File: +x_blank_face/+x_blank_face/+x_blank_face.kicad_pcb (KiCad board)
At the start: 2 copper layers, 87 x 326.5 mm, 14 parts

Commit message: added schematic to +x and routed ish the schematic
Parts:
- added J1: Conn_01x08_Pin, CNN_GNSS_Footprint:DF13-8P, F.Cu at (194.3, 5.54)
- added J2: Conn_01x02_Pin, CNN_GNSS_Footprint:TE_440055-2, F.Cu at (195.2, 160.1)
- added J3: Conn_01x02_Pin, CNN_GNSS_Footprint:TE_440055-2, F.Cu at (194.0, 57.5)
- added R1: 75, CNN_GNSS_Footprint:UB3C-75RF1, F.Cu at (201.5, 36.8)
- added R2: 75, CNN_GNSS_Footprint:UB3C-75RF1, F.Cu at (188.7, 37.2)
- added R3: 75, CNN_GNSS_Footprint:UB3C-75RF1, F.Cu at (186.1, 133.0)
- added R4: 75, CNN_GNSS_Footprint:UB3C-75RF1, F.Cu at (204.0, 132.7)
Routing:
- added copper zone on F.Cu, net /+X Drain
- added copper zone on B.Cu, net /12VPDM

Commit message: Updated panels based on dxf drawings from mech, need to move all holes up 5mm
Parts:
- J1: moved to B.Cu
- moved R4 70.0 mm to (177.3, 197.4)
- moved R3 65.7 mm to (173.2, 197.4)
- moved J3 55.2 mm to (173.5, 6.32)
- moved R1 27.3 mm to (177.3, 49.4)
- moved J2 22.7 mm to (173.6, 153.0), turned to 0 degrees
- moved R2 19.7 mm to (173.2, 49.4)
- moved J1 15.3 mm to (196.5, 20.7), turned to 180 degrees
- moved H14 6.56 mm to (234.1, 94.1)
- moved H10 6.54 mm to (157.9, 94.1)
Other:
- outline, holes or cut-outs redrawn
- board text added: "${REFERENCE}"

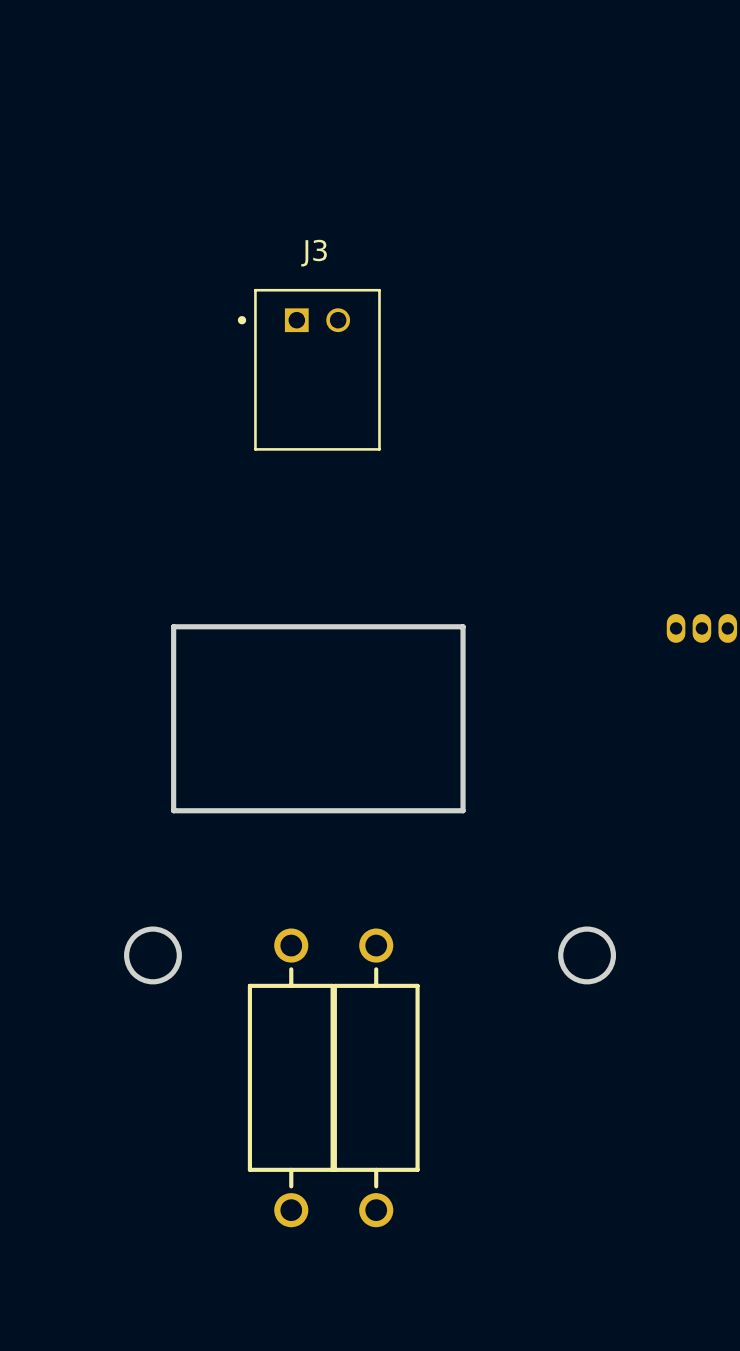
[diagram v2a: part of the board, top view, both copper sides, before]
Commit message: moved holes up 5mm, did what Jack said to do
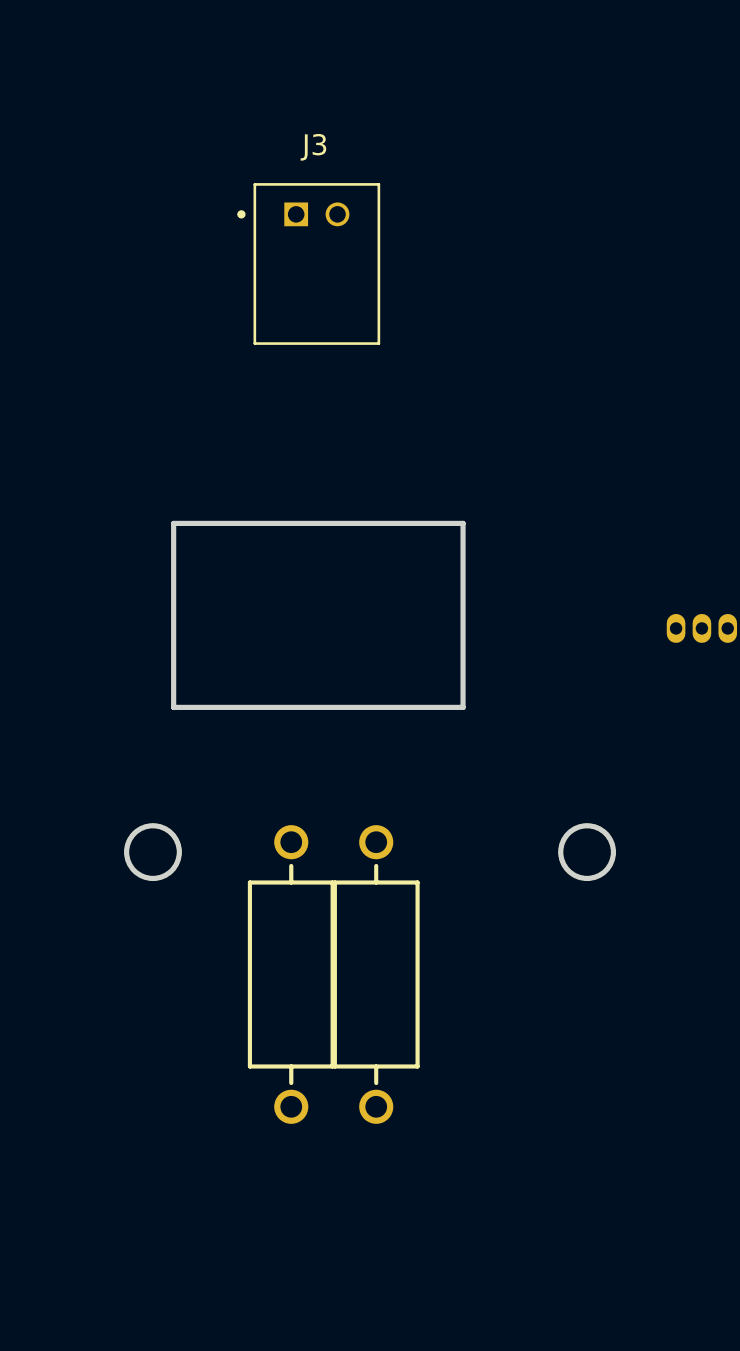
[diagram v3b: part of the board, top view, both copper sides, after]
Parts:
- moved J3 5.12 mm to (173.4, 1.20)
- moved R1 5.00 mm to (177.3, 44.4)
- moved R2 5.00 mm to (173.2, 44.4)
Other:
- outline, holes or cut-outs redrawn
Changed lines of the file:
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@@
 	(footprint "CNN_GNSS_Footprint:UB3C-75RF1"
 		(layer "F.Cu")
-		(at 177.31 49.371 90)
+		(at 177.31 44.371 90)
 		(descr "RES 50 OHM 1% 3W AXIAL")
 		(tags "Resistor")
@@
 	(footprint "CNN_GNSS_Footprint:UB3C-75RF1"
 		(layer "F.Cu")
-		(at 173.2 49.371 90)
+		(at 173.2 44.371 90)
 		(descr "RES 50 OHM 1% 3W AXIAL")
 		(tags "Resistor")
@@
 	(footprint "CNN_GNSS_Footprint:TE_440055-2"
 		(layer "F.Cu")
-		(at 173.4675 6.32)
+		(at 173.4375 1.2)
 		(property "Reference" "J3"
 			(at 0.925 -3.335 0)
@@
 	)
 	(gr_line
-		(start 167.51 21.15)
-		(end 181.51 21.15)
+		(start 167.51 16.15)
+		(end 181.51 16.15)
 		(stroke
 			(width 0.25)
@@
 	)
 	(gr_line
-		(start 181.51 30.05)
-		(end 181.51 21.15)
+		(start 181.51 25.05)
+		(end 181.51 16.15)
 		(stroke
 			(width 0.25)
@@
 	)
 	(gr_circle
-		(center 166.51 37.05)
-		(end 166.51 35.775)
+		(center 166.51 32.05)
+		(end 166.51 30.775)
 		(stroke
 			(width 0.25)
@@
 	)
 	(gr_circle
-		(center 187.51 37.05)
-		(end 187.51 35.775)
+		(center 187.51 32.05)
+		(end 187.51 30.775)
 		(stroke
 			(width 0.25)
@@
 	)
 	(gr_line
-		(start 167.51 30.05)
-		(end 181.51 30.05)
+		(start 167.51 25.05)
+		(end 181.51 25.05)
 		(stroke
 			(width 0.25)
@@
 	)
 	(gr_line
-		(start 167.51 30.05)
-		(end 167.51 21.15)
+		(start 167.51 25.05)
+		(end 167.51 16.15)
 		(stroke
 			(width 0.25)

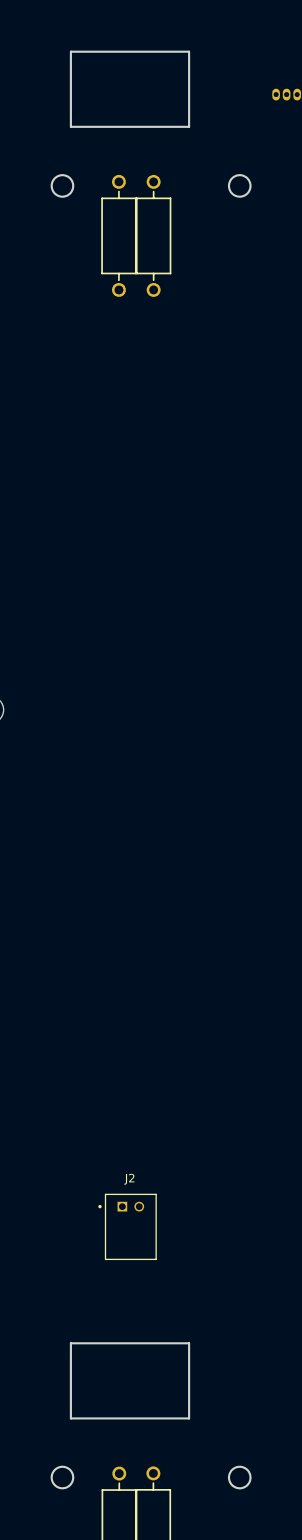
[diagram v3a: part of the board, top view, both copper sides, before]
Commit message: Moved some things around, locked some components
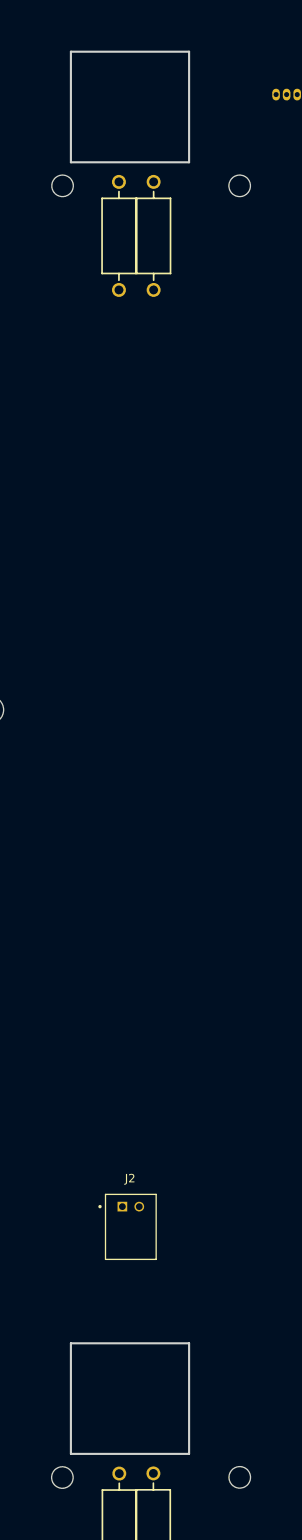
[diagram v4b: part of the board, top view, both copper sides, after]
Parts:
- added H1: MountingHole, CNN_GNSS_Footprint:2.55mm_Mounting_Hole, F.Cu at (187.5, 32.1)
- added H2: MountingHole, CNN_GNSS_Footprint:2.55mm_Mounting_Hole, F.Cu at (166.5, 32.1)
- added H3: MountingHole, CNN_GNSS_Footprint:2.55mm_Mounting_Hole, F.Cu at (166.5, 185.1)
- added H4: MountingHole, CNN_GNSS_Footprint:2.55mm_Mounting_Hole, F.Cu at (187.5, 185.1)
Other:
- outline, holes or cut-outs redrawn

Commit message: changed ALOT of things, got it to a point to send mech models,solar panel harness on BS need changed
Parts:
- J2, J3: moved to B.Cu
- moved J1 5.64 mm to (191.0, 21.7), turned to 0 degrees
- moved J3 5.30 mm to (175.8, -3.57), turned to 180 degrees
- moved J2 3.60 mm to (175.0, 149.7), turned to 180 degrees
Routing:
- net GND: track 0.00 -> 171.1 mm
- net /-X Serial Out: track 0.00 -> 169.8 mm

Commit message: I forgot what I changed
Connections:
- J1 pad 1: /12VPDM -> GND
- J1 pad 2: /12VPDM -> GND
- J1 pad 3: /+X Drain -> /-X Serial Out
- J1 pad 4: /+X Drain -> /-X Serial Out
- J1 pad 5: /-X Serial Out -> /+X Drain
- J1 pad 6: /-X Serial Out -> /+X Drain
- J1 pad 7: GND -> /12VPDM
- J1 pad 8: GND -> /12VPDM
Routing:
- net GND: track 171.1 -> 167.3 mm
- net /-X Serial Out: track 169.8 -> 168.3 mm
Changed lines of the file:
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@@
 			(remove_unused_layers no)
 			(roundrect_rratio 0.25)
-			(net 1 "/12VPDM")
+			(net 4 "GND")
 			(pinfunction "Pin_1")
 			(pintype "passive")
@@
 			(layers "*.Cu" "*.Mask")
 			(remove_unused_layers no)
-			(net 1 "/12VPDM")
+			(net 4 "GND")
 			(pinfunction "Pin_2")
 			(pintype "passive")
@@
 			(layers "*.Cu" "*.Mask")
 			(remove_unused_layers no)
-			(net 3 "/+X Drain")
+			(net 2 "/-X Serial Out")
 			(pinfunction "Pin_3")
 			(pintype "passive")
@@
 			(layers "*.Cu" "*.Mask")
 			(remove_unused_layers no)
-			(net 3 "/+X Drain")
+			(net 2 "/-X Serial Out")
 			(pinfunction "Pin_4")
 			(pintype "passive")
@@
 			(layers "*.Cu" "*.Mask")
 			(remove_unused_layers no)
-			(net 2 "/-X Serial Out")
+			(net 3 "/+X Drain")
 			(pinfunction "Pin_5")
 			(pintype "passive")
@@
 			(layers "*.Cu" "*.Mask")
 			(remove_unused_layers no)
-			(net 2 "/-X Serial Out")
+			(net 3 "/+X Drain")
 			(pinfunction "Pin_6")
 			(pintype "passive")
@@
 			(layers "*.Cu" "*.Mask")
 			(remove_unused_layers no)
-			(net 4 "GND")
+			(net 1 "/12VPDM")
 			(pinfunction "Pin_7")
 			(pintype "passive")
@@
 			(layers "*.Cu" "*.Mask")
 			(remove_unused_layers no)
-			(net 4 "GND")
+			(net 1 "/12VPDM")
 			(pinfunction "Pin_8")
 			(pintype "passive")
@@
 	)
 	(segment
-		(start 173.0325 149.65)
-		(end 191.89 130.7925)
+		(start 189.435 21.18)
+		(end 190.685 21.18)
+		(width 0.2)
+		(layer "F.Cu")
+		(net 2)
+	)
+	(segment
+		(start 173.0325 149.6375)
+		(end 190.585 132.085)
 		(width 0.2)
 		(layer "B.Cu")
@@
 	)
 	(segment
+		(start 190.685 131.985)
+		(end 190.585 132.085)
+		(width 0.2)
+		(layer "B.Cu")
+		(net 2)
+	)
+	(segment
+		(start 189.435 18.227926)
+		(end 189.435 21.18)
+		(width 0.2)
+		(layer "B.Cu")
+		(net 2)
+	)
+	(segment
 		(start 173.7525 -3.57)
 		(end 173.7525 2.545426)
@@
 	)
 	(segment
-		(start 191.935 21.18)
-		(end 193.185 21.18)
+		(start 173.7525 2.545426)
+		(end 189.435 18.227926)
 		(width 0.2)
 		(layer "B.Cu")
@@
 	)
 	(segment
-		(start 191.89 130.7925)
-		(end 191.89 21.655)
+		(start 190.685 21.18)
+		(end 190.685 131.985)
 		(width 0.2)
 		(layer "B.Cu")
@@
 	)
 	(segment
-		(start 191.935 20.727926)
-		(end 173.7525 2.545426)
+		(start 173.0325 149.65)
+		(end 173.0325 149.6375)
 		(width 0.2)
 		(layer "B.Cu")
@@
 	(segment
 		(start 191.935 21.18)
-		(end 191.935 20.727926)
+		(end 191.935 21.61)
 		(width 0.2)
 		(layer "B.Cu")
-		(net 2)
-	)
-	(segment
-		(start 191.935 21.18)
-		(end 191.935 21.61)
-		(width 0.2)
-		(layer "B.Cu")
-		(net 2)
+		(net 3)
 	)
 	(segment
@@
 		(width 0.2)
 		(layer "B.Cu")
-		(net 2)
-	)
-	(segment
-		(start 194.435 21.18)
-		(end 195.685 21.18)
-		(width 0.2)
-		(layer "B.Cu")
+		(net 3)
+	)
+	(segment
+		(start 192.42 132.2625)
+		(end 192.42 26.665)
+		(width 0.2)
+		(layer "F.Cu")
 		(net 4)
 	)
 	(segment
-		(start 175.75 1.36)
-		(end 194.435 20.045)
-		(width 0.2)
-		(layer "B.Cu")
+		(start 192.42 26.665)
+		(end 186.935 21.18)
+		(width 0.2)
+		(layer "F.Cu")
 		(net 4)
 	)
 	(segment
-		(start 176.47 149.65)
-		(end 194.435 131.685)
-		(width 0.2)
-		(layer "B.Cu")
+		(start 175.7525 -3.57)
+		(end 175.7525 2.2525)
+		(width 0.2)
+		(layer "F.Cu")
 		(net 4)
 	)
 	(segment
-		(start 194.435 21.18)
-		(end 194.435 131.685)
-		(width 0.2)
-		(layer "B.Cu")
+		(start 175.7525 2.2525)
+		(end 186.935 13.435)
+		(width 0.2)
+		(layer "F.Cu")
 		(net 4)
 	)
 	(segment
-		(start 175.7525 -3.57)
-		(end 175.7525 1.3575)
-		(width 0.2)
-		(layer "B.Cu")
+		(start 186.935 13.435)
+		(end 186.935 21.18)
+		(width 0.2)
+		(layer "F.Cu")
 		(net 4)
 	)
 	(segment
-		(start 175.7525 1.3575)
-		(end 175.75 1.36)
-		(width 0.2)
-		(layer "B.Cu")
+		(start 175.0325 149.65)
+		(end 192.42 132.2625)
+		(width 0.2)
+		(layer "F.Cu")
 		(net 4)
 	)
-	(segment
-		(start 175.0325 149.65)
-		(end 176.47 149.65)
-		(width 0.2)
-		(layer "B.Cu")
-		(net 4)
-	)
-	(segment
-		(start 194.435 20.045)
-		(end 194.435 21.18)
-		(width 0.2)
-		(layer "B.Cu")
-		(net 4)
-	)

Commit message: Rerouted some stuff
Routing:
- net /-X Serial Out: track 168.3 -> 165.3 mm
- net GND: track 167.3 -> 166.2 mm

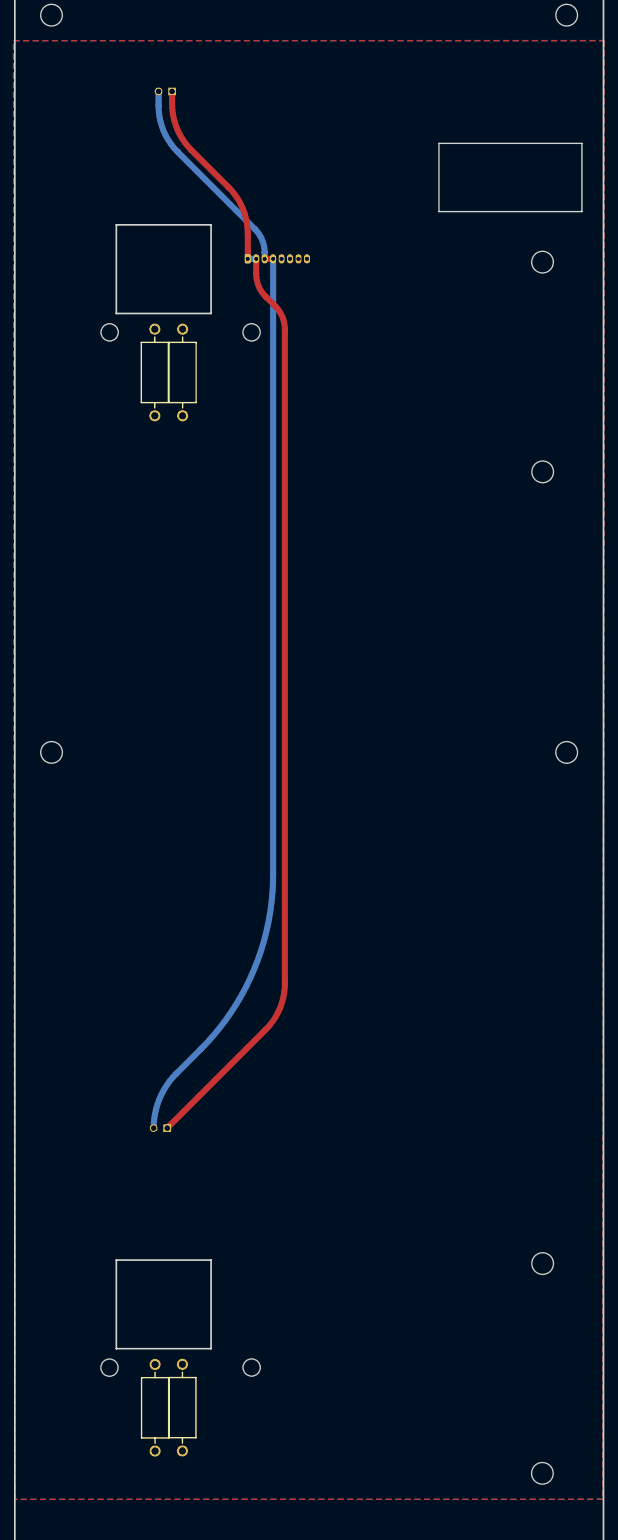
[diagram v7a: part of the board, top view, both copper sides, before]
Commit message: Removed GND and PWR plane, replaced with traces, switches are now in series rather than in parallel
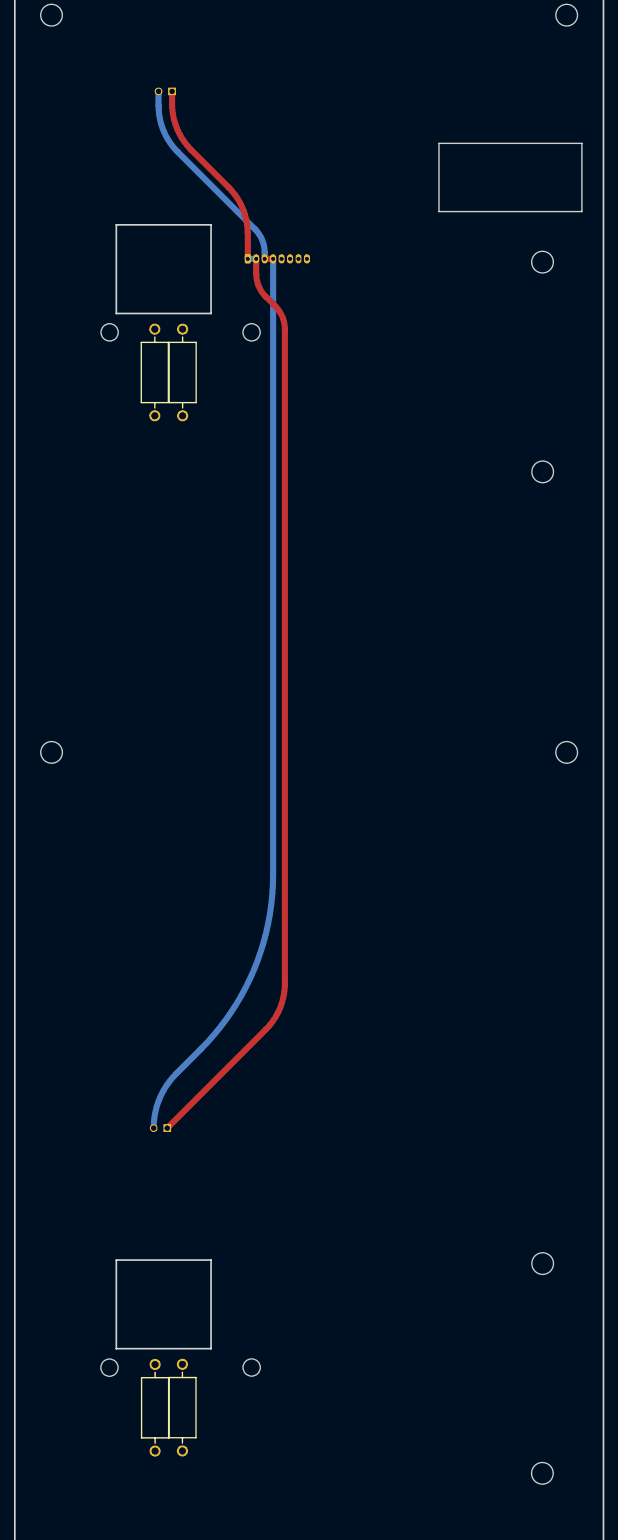
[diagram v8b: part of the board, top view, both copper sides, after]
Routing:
- removed copper zone on F.Cu, net /+X Drain
- removed copper zone on B.Cu, net /12VPDM
